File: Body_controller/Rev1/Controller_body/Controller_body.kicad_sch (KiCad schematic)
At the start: 23 parts, among them J1 Conn_01x06_Socket, J2 Conn_01x03_Socket, U1 PCF8575PWR

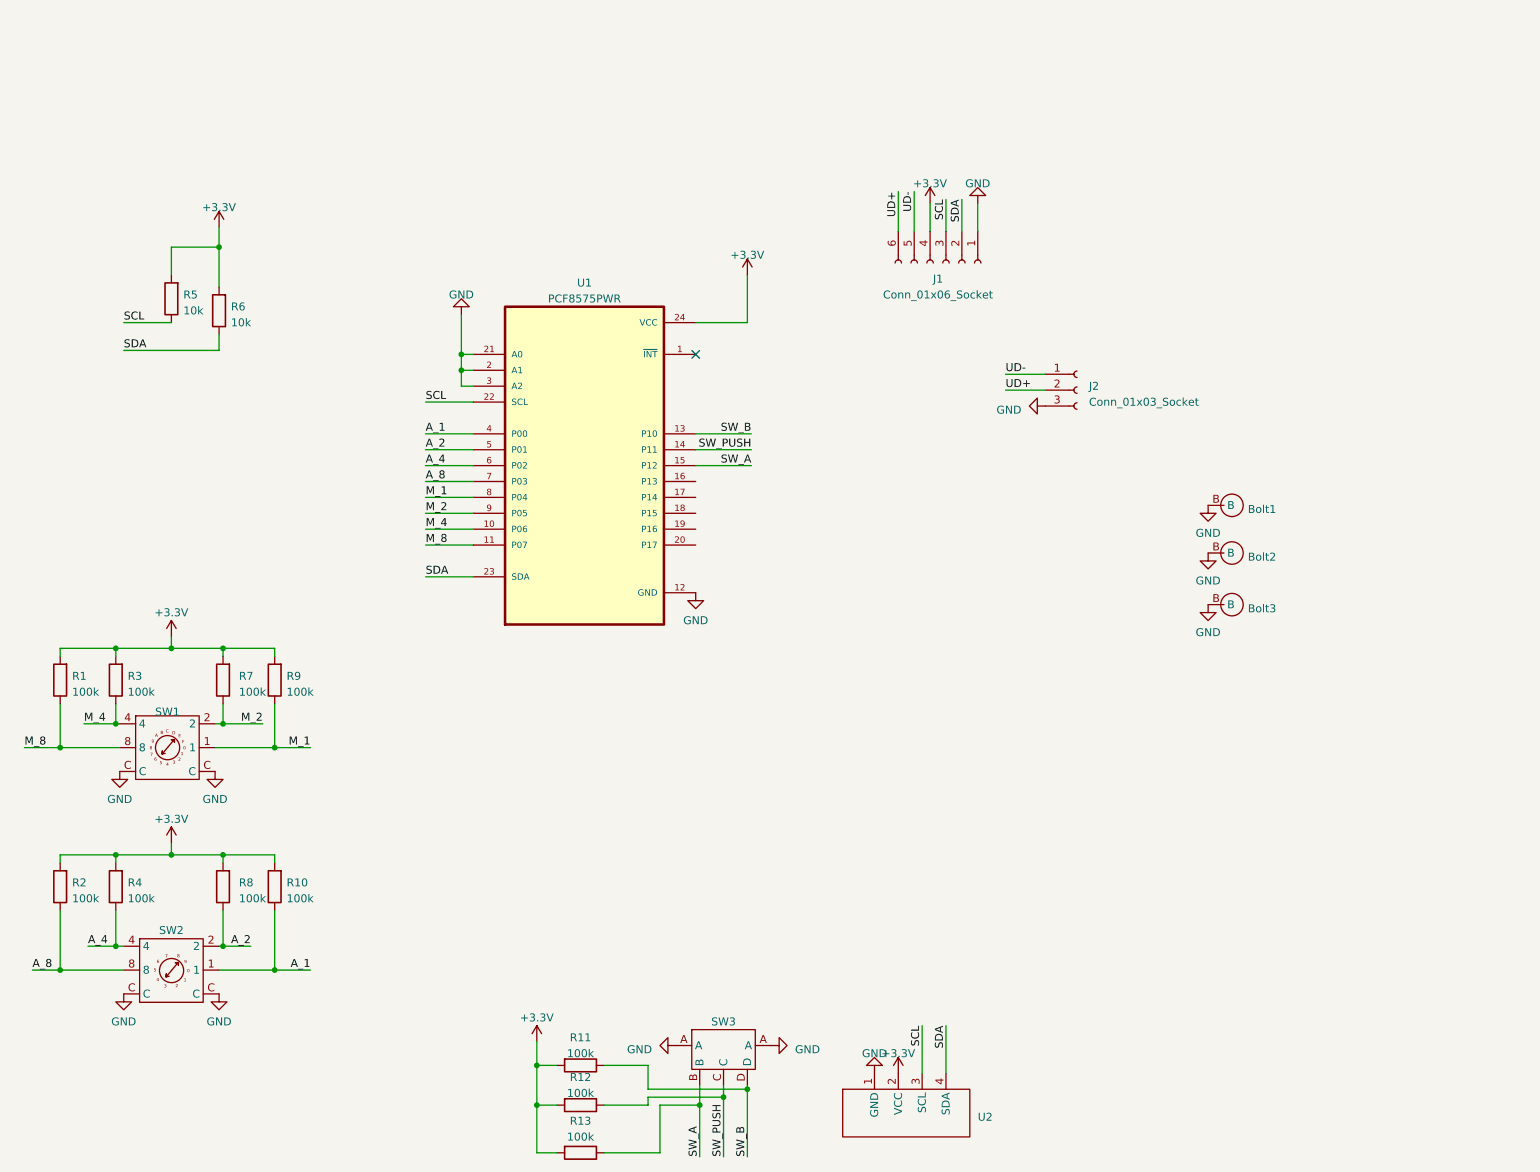
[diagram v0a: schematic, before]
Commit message: update to Kicad 8.0 & update BodyController to Rev 2.0
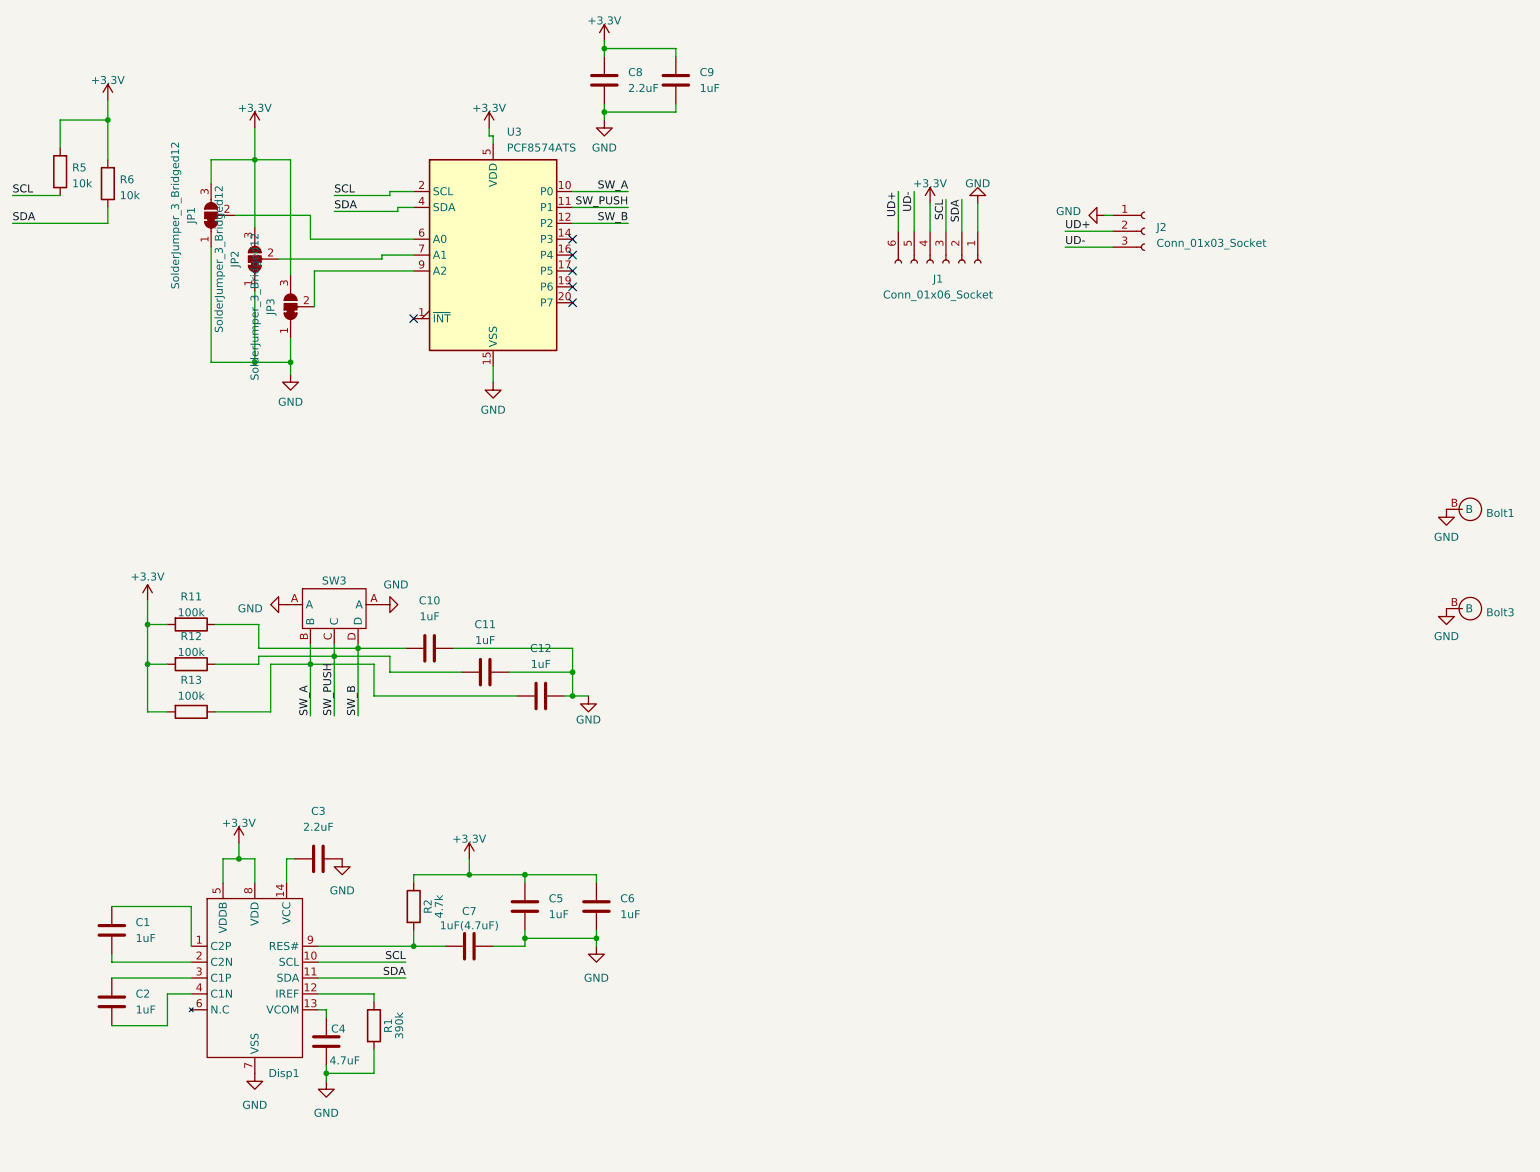
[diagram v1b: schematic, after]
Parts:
- removed Bolt2: ~, 0JIMMY:M3_Bolt, symbol 0JIMMY:M3_Bolt
- removed R10, R3, R4, R7, R8, R9: 100k, Resistor_SMD:R_0805_2012Metric_Pad1.20x1.40mm_HandSolder, symbol Device:R
- removed SW1: ~, SW_CODED:GSMR_16, symbol CODED_SW:GSMR16
- removed SW2: ~, SW_CODED:GSMR_10S, symbol CODED_SW:GSMR10S
- removed U1: PCF8575PWR, SOP65P640X120-24N, symbol PCF8575PWR:PCF8575PWR
- removed U2: ~, 0JIMMY:OLED 0.96 i2c, symbol 0JIMMY:OLED_0.96''_i2c
- added C1, C10, C11, C12, C2, C5, C6, C9: 1uF, Capacitor_SMD:C_0603_1608Metric_Pad1.08x0.95mm_HandSolder, symbol Device:C
- added C3, C8: 2.2uF, Capacitor_SMD:C_0603_1608Metric_Pad1.08x0.95mm_HandSolder, symbol Device:C
- added C4: 4.7uF, Capacitor_SMD:C_0603_1608Metric_Pad1.08x0.95mm_HandSolder, symbol Device:C
- added C7: 1uF(4.7uF), Capacitor_SMD:C_0603_1608Metric_Pad1.08x0.95mm_HandSolder, symbol Device:C
- added Disp1: ~, KiCadLib:SSD1306_0.91_i2c, symbol KiCadLib:Oled_128_32_Raw
- added JP1, JP2, JP3: SolderJumper_3_Bridged12, Jumper:SolderJumper-3_P1.3mm_Bridged12_RoundedPad1.0x1.5mm_NumberLabels, symbol Jumper:SolderJumper_3_Bridged12
- added U3: PCF8574ATS, Package_SO:SSOP-20_4.4x6.5mm_P0.65mm, symbol Interface_Expansion:PCF8574ATS
- R1: value 100k -> 390k; footprint Resistor_SMD:R_0805_2012Metric_Pad1.20x1.40mm_HandSolder -> Resistor_SMD:R_0603_1608Metric_Pad0.98x0.95mm_HandSolder
- R11, R12, R13: footprint Resistor_SMD:R_0805_2012Metric_Pad1.20x1.40mm_HandSolder -> Resistor_SMD:R_0603_1608Metric_Pad0.98x0.95mm_HandSolder
- R2: value 100k -> 4.7k; footprint Resistor_SMD:R_0805_2012Metric_Pad1.20x1.40mm_HandSolder -> Resistor_SMD:R_0603_1608Metric_Pad0.98x0.95mm_HandSolder
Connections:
- net A_8 is gone; now on net +3.3V: R2.1
- net +3.3V: now also C5.1, C6.1, C8.1, C9.1, Disp1.5 (VDDB), Disp1.8 (VDD), JP1.3 (B), JP2.3 (B), JP3.3 (B), U3.5 (VDD); no longer R1.2, R2.2
- net GND: now also J2.1 (Pin_1), R1.2, C10.2, C11.2, C12.2, C3.2, C4.1, C5.2, C6.2, C7.2, C8.2, C9.2, Disp1.7 (VSS), JP1.1 (A), JP2.1 (A), JP3.1 (A), U3.15 (VSS); no longer J2.3 (Pin_3)
- net SCL: now also Disp1.10 (SCL), U3.2 (SCL)
- net SDA: now also Disp1.11 (SDA), U3.4 (SDA)
- net SW_A: now also C12.1, U3.10 (P0)
- net SW_B: now also C10.1, U3.12 (P2)
- net SW_PUSH: now also C11.1, U3.11 (P1)
- net UD-: now also J2.3 (Pin_3); no longer J2.1 (Pin_1)
- net M_8: no longer names the net of R1.1
- net M_8: now also Disp1.12 (IREF)
- new net: C4.2, Disp1.13 (VCOM)
- new net: C1.1, Disp1.1 (C2P)
- new net: C3.1, Disp1.14 (VCC)
- new net: C1.2, Disp1.2 (C2N)
- new net: C2.1, Disp1.3 (C1P)
- new net: C2.2, Disp1.4 (C1N)
- new net: C7.1, Disp1.9 (RES#), R2.2
- new net: JP2.2 (C), U3.7 (A1)
- new net: JP1.2 (C), U3.6 (A0)
- new net: JP3.2 (C), U3.9 (A2)
- no-connect marks 1 -> 6
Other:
- moved on the sheet: Bolt1, Bolt3, J2, R11, R12, R13, R5, R6, SW3
